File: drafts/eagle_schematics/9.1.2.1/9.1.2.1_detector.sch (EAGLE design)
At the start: 14 parts, among them IC1 LMV393D, Q1 CSD88539ND, Q2 CSD88539ND, Q3 2N7002

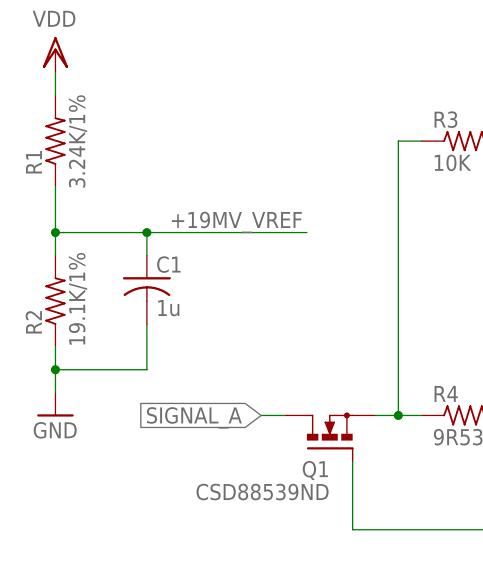
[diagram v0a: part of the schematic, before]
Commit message: Fix schematic error.
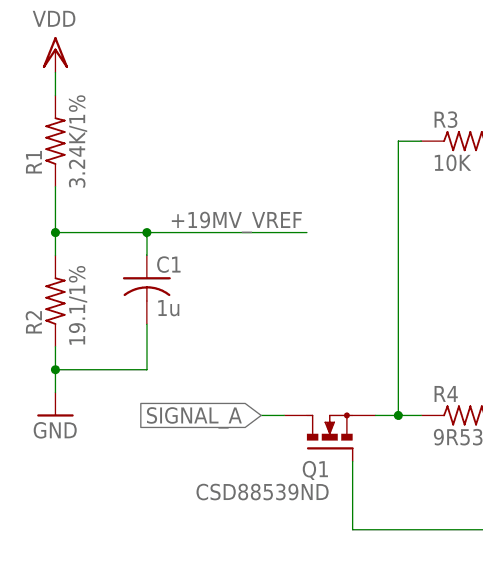
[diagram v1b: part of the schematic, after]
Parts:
- R2: value 19.1K/1% -> 19.1/1%
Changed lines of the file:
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@@
 <part name="C1" library="rcl" library_urn="urn:adsk.eagle:library:334" deviceset="C-US" device="C0402" package3d_urn="urn:adsk.eagle:package:23626/2" value="1u"/>
 <part name="R1" library="resistor" library_urn="urn:adsk.eagle:library:348" deviceset="R-US_" device="R0402" package3d_urn="urn:adsk.eagle:package:26058/1" value="3.24K/1%"/>
-<part name="R2" library="resistor" library_urn="urn:adsk.eagle:library:348" deviceset="R-US_" device="R0402" package3d_urn="urn:adsk.eagle:package:26058/1" value="19.1K/1%"/>
+<part name="R2" library="resistor" library_urn="urn:adsk.eagle:library:348" deviceset="R-US_" device="R0402" package3d_urn="urn:adsk.eagle:package:26058/1" value="19.1/1%"/>
 <part name="GND6" library="supply1" library_urn="urn:adsk.eagle:library:371" deviceset="GND" device=""/>
 <part name="VDD3" library="supply1" library_urn="urn:adsk.eagle:library:371" deviceset="VDD" device=""/>

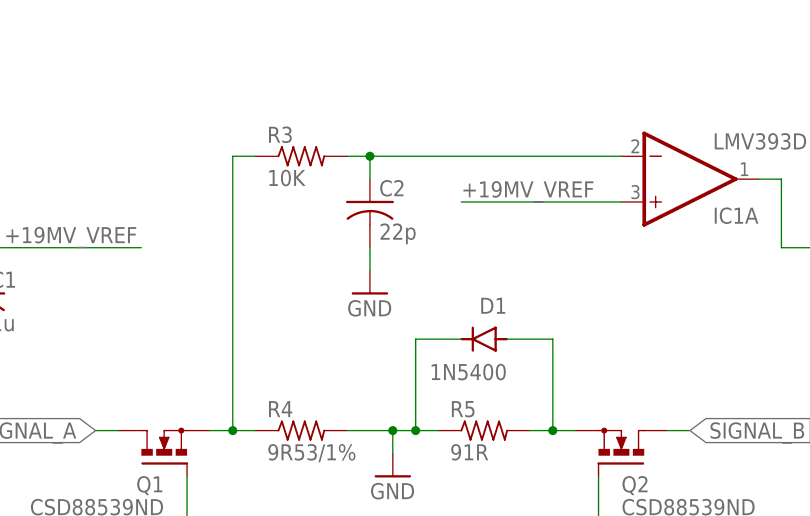
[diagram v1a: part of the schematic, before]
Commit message: Update RailCom reference circuits.
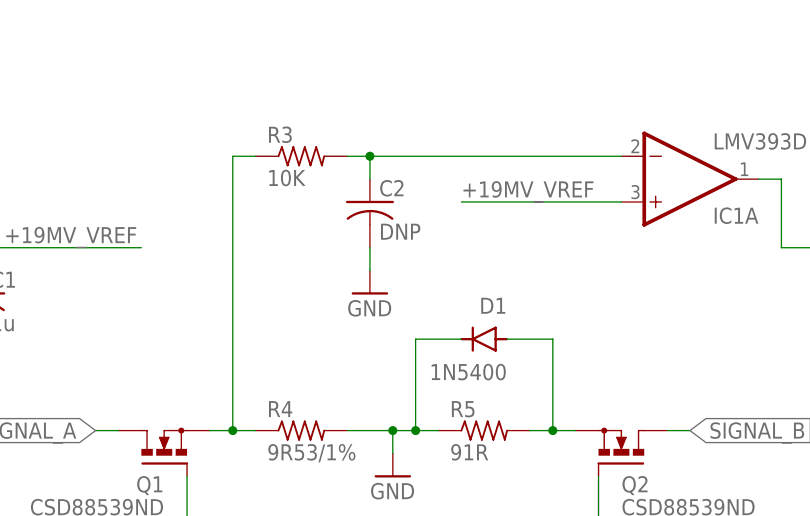
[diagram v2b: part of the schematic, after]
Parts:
- C2: value 22p -> DNP
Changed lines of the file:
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@@
 <?xml version="1.0" encoding="utf-8"?>
 <!DOCTYPE eagle SYSTEM "eagle.dtd">
-<eagle version="9.6.0">
+<eagle version="9.6.2">
 <drawing>
 <settings>
-<setting alwaysvectorfont="yes"/>
+<setting alwaysvectorfont="no"/>
 <setting verticaltext="up"/>
 </settings>
@@
 <part name="R5" library="resistor" library_urn="urn:adsk.eagle:library:348" deviceset="R-US_" device="R1206" package3d_urn="urn:adsk.eagle:package:26062/1" value="91R"/>
 <part name="R3" library="resistor" library_urn="urn:adsk.eagle:library:348" deviceset="R-US_" device="R0402" package3d_urn="urn:adsk.eagle:package:26058/1" value="10K"/>
-<part name="C2" library="rcl" library_urn="urn:adsk.eagle:library:334" deviceset="C-US" device="C0402" package3d_urn="urn:adsk.eagle:package:23626/2" value="22p"/>
+<part name="C2" library="rcl" library_urn="urn:adsk.eagle:library:334" deviceset="C-US" device="C0402" package3d_urn="urn:adsk.eagle:package:23626/2" value="DNP"/>
 <part name="P+1" library="supply1" library_urn="urn:adsk.eagle:library:371" deviceset="+12V" device=""/>
 <part name="Q3" library="transistor-power" library_urn="urn:adsk.eagle:library:400" deviceset="IRF512" device="" package3d_urn="urn:adsk.eagle:package:29484/3" value="2N7002"/>
